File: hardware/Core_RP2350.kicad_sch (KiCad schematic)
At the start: 69 parts, among them J1 5-146281-3, J2 5-146281-3, J3 AudioJack3, J4 USB_C_Receptacle_USB2.0, J5 Micro_SD_Card_Det_Hirose_DM3AT, SW2 SPST-NO, U2 W25Q16JVUXIQ, U3 ADUM4160, U32 RP2350_80QFN

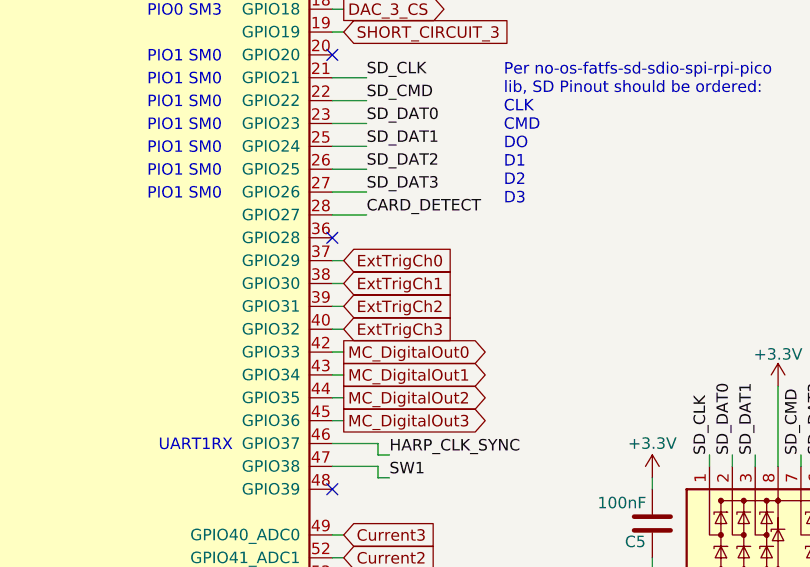
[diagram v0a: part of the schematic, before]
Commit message: flip c12; put ext triggers on gpio multiple of 8
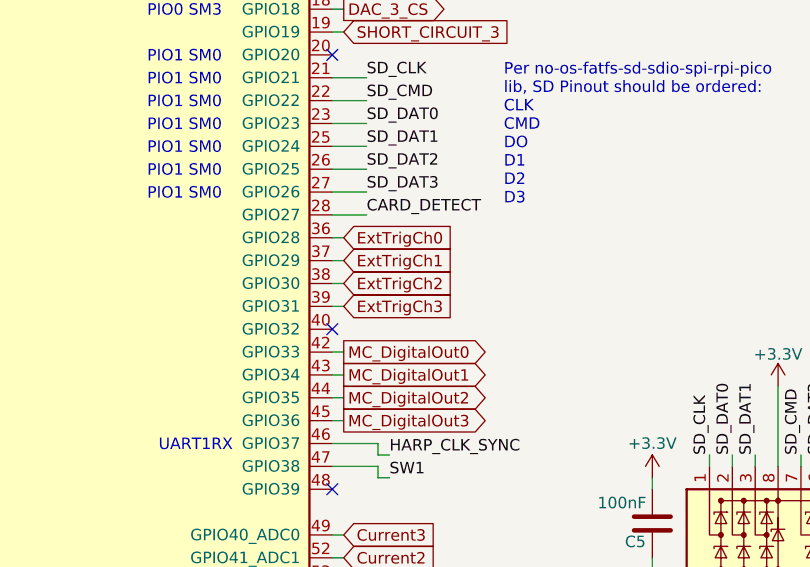
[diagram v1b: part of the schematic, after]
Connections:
- net ExtTrigCh0: now also U32.36 (GPIO28); no longer U32.37 (GPIO29)
- net ExtTrigCh1: now also U32.37 (GPIO29); no longer U32.38 (GPIO30)
- net ExtTrigCh2: now also U32.38 (GPIO30); no longer U32.39 (GPIO31)
- net ExtTrigCh3: now also U32.39 (GPIO31); no longer U32.40 (GPIO32)
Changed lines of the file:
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@@
 	)
 	(no_connect
-		(at 134.62 113.03)
+		(at 134.62 123.19)
 	)
 	(no_connect
@@
 	(wire
 		(pts
-			(xy 134.62 120.65) (xy 135.89 120.65)
+			(xy 134.62 118.11) (xy 135.89 118.11)
 		)
 		(stroke
@@
 	(wire
 		(pts
-			(xy 134.62 123.19) (xy 135.89 123.19)
+			(xy 134.62 120.65) (xy 135.89 120.65)
 		)
 		(stroke
@@
 	(wire
 		(pts
-			(xy 134.62 115.57) (xy 135.89 115.57)
+			(xy 134.62 113.03) (xy 135.89 113.03)
 		)
 		(stroke
@@
 	(wire
 		(pts
-			(xy 134.62 118.11) (xy 135.89 118.11)
+			(xy 134.62 115.57) (xy 135.89 115.57)
 		)
 		(stroke
@@
 	(global_label "ExtTrigCh2"
 		(shape input)
-		(at 135.89 120.65 0)
+		(at 135.89 118.11 0)
 		(fields_autoplaced yes)
 		(effects
@@
 		)
 		(property "Intersheetrefs" "${INTERSHEET_REFS}"
-			(at 148.9141 120.65 0)
+			(at 148.9141 118.11 0)
 			(effects
 				(font
@@
 	(global_label "ExtTrigCh3"
 		(shape input)
-		(at 135.89 123.19 0)
+		(at 135.89 120.65 0)
 		(fields_autoplaced yes)
 		(effects
@@
 		)
 		(property "Intersheetrefs" "${INTERSHEET_REFS}"
-			(at 148.9141 123.19 0)
+			(at 148.9141 120.65 0)
 			(effects
 				(font
@@
 	(global_label "ExtTrigCh1"
 		(shape input)
-		(at 135.89 118.11 0)
+		(at 135.89 115.57 0)
 		(fields_autoplaced yes)
 		(effects
@@
 		)
 		(property "Intersheetrefs" "${INTERSHEET_REFS}"
-			(at 148.9141 118.11 0)
+			(at 148.9141 115.57 0)
 			(effects
 				(font
@@
 	(global_label "ExtTrigCh0"
 		(shape input)
-		(at 135.89 115.57 0)
+		(at 135.89 113.03 0)
 		(fields_autoplaced yes)
 		(effects
@@
 		)
 		(property "Intersheetrefs" "${INTERSHEET_REFS}"
-			(at 148.9141 115.57 0)
+			(at 148.9141 113.03 0)
 			(effects
 				(font
@@
 		)
 		(instances
-			(project ""
+			(project "harp.device.quad.dac"
 				(path "/6b47c519-21c4-43bd-9777-b273999e4447/5973743b-c3fc-4963-acef-26c8fa426708"
 					(reference "D29")
@@
 		)
 		(instances
-			(project ""
+			(project "harp.device.quad.dac"
 				(path "/6b47c519-21c4-43bd-9777-b273999e4447/5973743b-c3fc-4963-acef-26c8fa426708"
 					(reference "D5")
@@
 		)
 		(instances
-			(project ""
+			(project "harp.device.quad.dac"
 				(path "/6b47c519-21c4-43bd-9777-b273999e4447/5973743b-c3fc-4963-acef-26c8fa426708"
 					(reference "U32")
@@
 		)
 		(instances
-			(project ""
+			(project "harp.device.quad.dac"
 				(path "/6b47c519-21c4-43bd-9777-b273999e4447/5973743b-c3fc-4963-acef-26c8fa426708"
 					(reference "J5")

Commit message: add pulldowns to external triggers
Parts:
- R5: Tolerance 0.1% -> (none)

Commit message: change R3, R15, R16, R20, R21 package to 0402
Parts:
- R15, R16, R20, R21, R3: footprint Resistor_SMD:R_0603_1608Metric -> Resistor_SMD:R_0402_1005Metric
- R76, R77: PCBWay Link https://www.pcbway.com/components/detail/RC0402FR0727RL/656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 -> (none)
